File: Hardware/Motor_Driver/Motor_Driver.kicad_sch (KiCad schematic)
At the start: 16 parts, among them J1 Conn_SENSORS, J2 Conn_MOTOR, J3 Conn_MB, J4 Conn_PWR, Q1 CSD87333Q3D, Q2 CSD87333Q3D, Q3 CSD87333Q3D, U1 DRV8323SRTAR

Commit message: Day 4
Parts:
- removed Q1, Q2, Q3: CSD87333Q3D, Package_SON:VSON-8-1EP_3x3mm_P0.65mm_EP1.65x2.4mm, symbol Transistor_FET:DMN32D2LDF
- removed U1: DRV8323SRTAR, RTA0040B, symbol Driver_Motor:DRV8323SRTAR
- added C10, C11, C12, C13, C14, C15, C7, C8, C9: 4.7uF, symbol Device:C
- added C16, C17: C, symbol Device:C
- added D1: D_Schottky, symbol Device:D_Schottky
- added L1: L, symbol Device:L
- added Q1, Q2, Q3: CSD87333Q3D, Package_TO_SOT_SMD:SOT-353_SC-70-5, symbol Transistor_FET:CSD87333Q3D
- added R3, R4: R, symbol Device:R
- added U1: DRV8323RSRGZR, RTA0040B, symbol Driver_Motor:DRV8323RSRGZR
- C1, C2, C3, C5, C6, R1, R2: footprint (none) -> Capacitor_SMD:C_0402_1005Metric
- C4: footprint (none) -> Capacitor_SMD:C_0603_1608Metric
- J1: footprint (none) -> Connector_JST:JST_ZH_B6B-ZR_1x06_P1.50mm_Vertical
- J2: footprint (none) -> Connector_Pin:Pin_Bullet_D4.7mm
- J3: footprint (none) -> Connector_PinHeader_2.54mm:PinHeader_2x06_P2.54mm_Vertical
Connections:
- net +3V3: now also C5.1, U1.26 (VREF), U1.34 (CAL), U1.36 (DVDD); no longer J3.1 (Pin_1)
- net +5V: now also J3.1 (Pin_1), C17.1, L1.2, R3.1
- net BRAKE: now also U1.42 (INLC)
- net CLK: now also U1.31 (SCLK)
- net CS: now also U1.32 (nSCS)
- net DIR: now also U1.41 (INHC)
- net EN: now also U1.33 (ENABLE)
- net FAULT: now also U1.28 (nFAULT)
- net GND: now also C10.2, C11.2, C12.2, C13.2, C14.2, C15.2, C7.2, C8.2, C9.2, D1.2 (A), Q1.9 (P_{GND}), Q2.9 (P_{GND}), Q3.9 (P_{GND}), R4.2, U1.2 (PGND), U1.27 (DGND), U1.35 (AGND), U1.43 (BGND)
- net HALL_A: now also U1.38 (INLA)
- net HALL_B: now also U1.39 (INHB)
- net HALL_C: now also U1.40 (INLB)
- net PWM: now also U1.37 (INHA)
- net SDI: now also U1.30 (SDI)
- net SDO: now also U1.29 (SDO)
- net VM: now reaches C2.1, C3.1, C4.1, J4.1 (Pin_1)
- net VM: now also C10.1, C11.1, C12.1, C13.1, C14.1, C15.1, C7.1, C8.1, C9.1, Q1.1 (V_{IN}), Q1.2 (V_{IN}), Q2.1 (V_{IN}), Q2.2 (V_{IN}), Q3.1 (V_{IN}), Q3.2 (V_{IN}), U1.6 (VM), U1.7 (VDRAIN)
- net at J2.2 (Pin_2): now also Q2.6 (V_{SW}), Q2.7 (V_{SW}), Q2.8 (V_{SW})
- net at C1.1: now also U1.4 (CPH)
- net at C1.2: now also U1.3 (CPL)
- net at J2.1 (Pin_1): now also Q1.6 (V_{SW}), Q1.7 (V_{SW}), Q1.8 (V_{SW})
- net at J2.3 (Pin_3): now also Q3.6 (V_{SW}), Q3.7 (V_{SW}), Q3.8 (V_{SW})
- net at C2.2: now also U1.5 (VCP)
- new net: R3.2, R4.1, U1.1 (FB)
- new net: Q1.3 (T_{G}), U1.8 (GHA)
- new net: Q1.4 (T_{GR}), U1.9 (SHA)
- new net: Q1.5 (B_{G}), U1.10 (GLA)
- new net: Q2.5 (B_{G}), U1.15 (GLB)
- new net: Q2.4 (T_{GR}), U1.16 (SHB)
- new net: Q2.3 (T_{G}), U1.17 (GHB)
- new net: Q3.3 (T_{G}), U1.18 (GHC)
- new net: Q3.4 (T_{GR}), U1.19 (SHC)
- new net: Q3.5 (B_{G}), U1.20 (GLC)
- new net: C16.1, U1.44 (CB)
- new net: C16.2, D1.1 (K), L1.1, U1.45 (SW)
- no-connect marks 9 -> 10
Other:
- moved on the sheet: J1

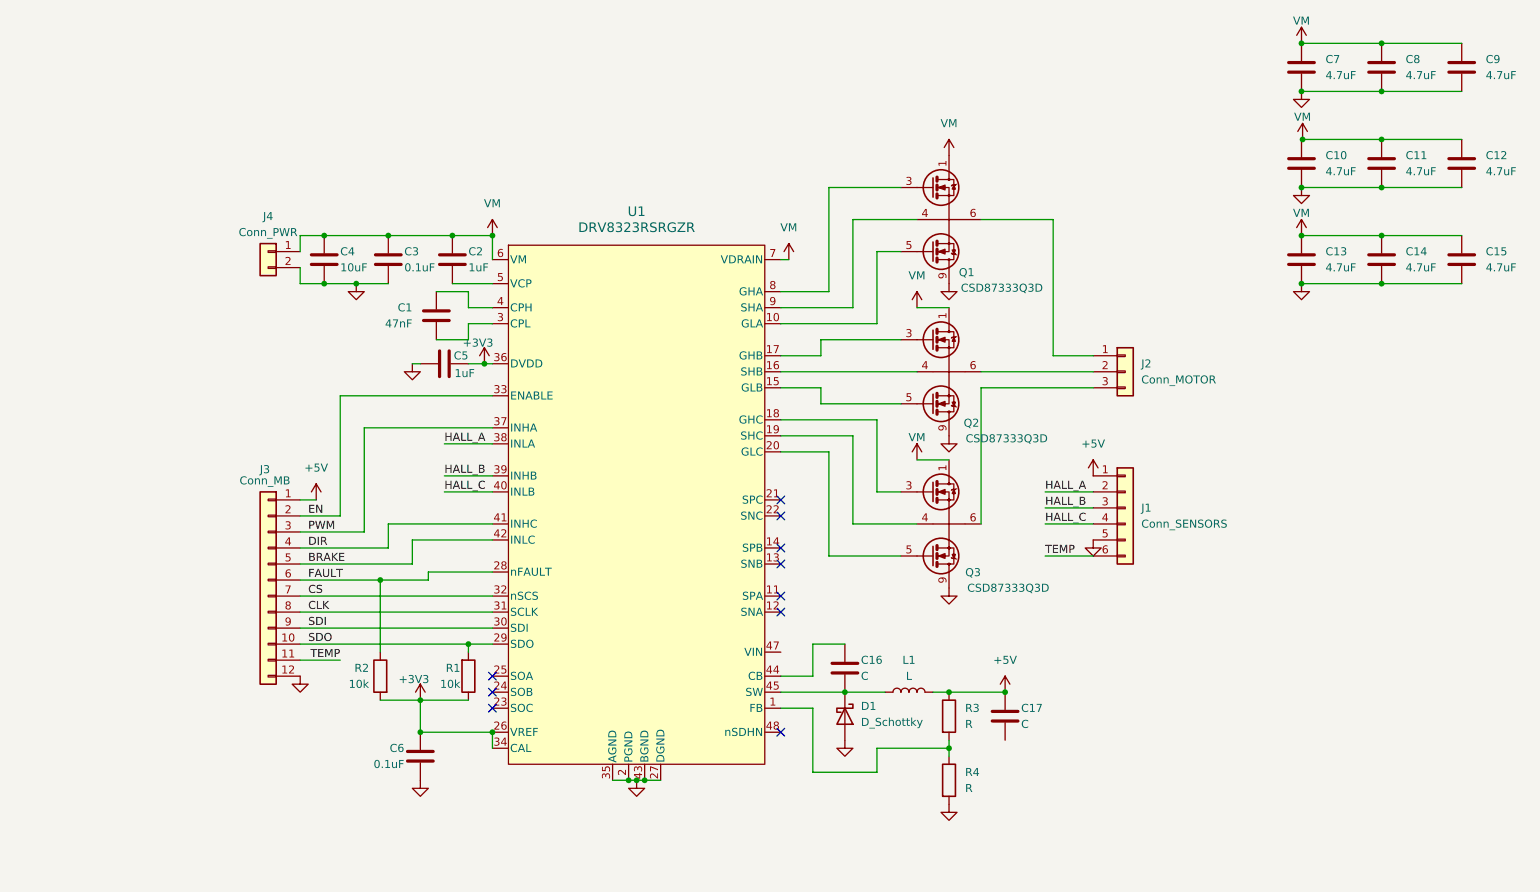
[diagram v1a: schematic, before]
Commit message: Day 5 - Finish motor driver PCB
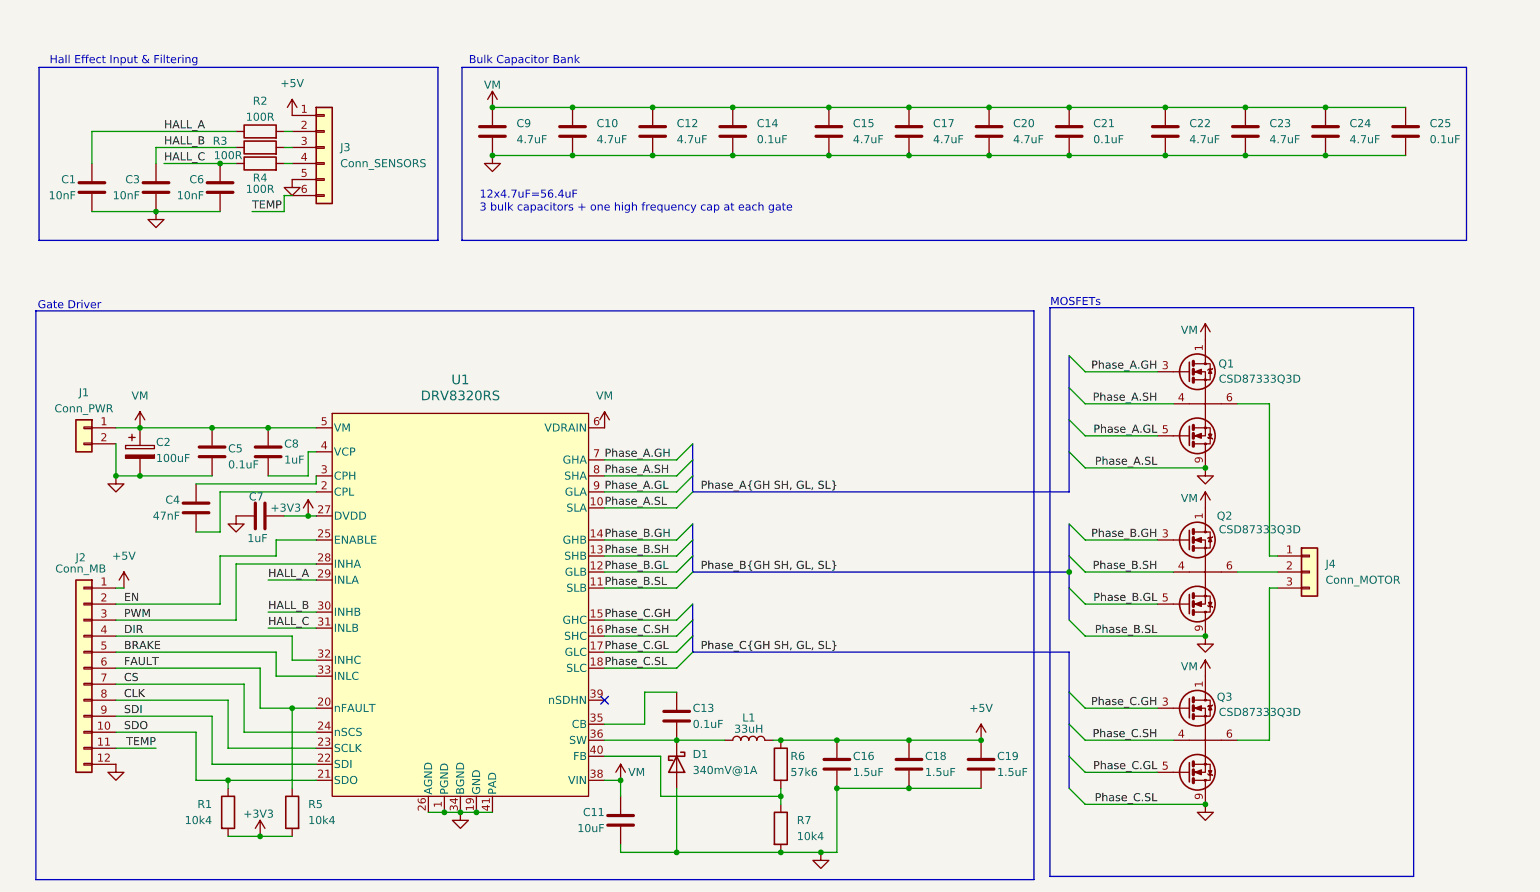
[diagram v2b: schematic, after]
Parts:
- removed C2: 1uF, Capacitor_SMD:C_0402_1005Metric, symbol Device:C
- removed U1: DRV8323RSRGZR, RTA0040B, symbol Driver_Motor:DRV8323RSRGZR
- added C11: 10uF, Capacitor_SMD:C_0603_1608Metric, symbol Device:C
- added C14, C21, C25: 0.1uF, Capacitor_SMD:C_0603_1608Metric, symbol Device:C
- added C18, C19: 1.5uF, Capacitor_SMD:C_0603_1608Metric, symbol Device:C
- added C2: 100uF, Capacitor_SMD:CP_Elec_10x10, symbol Device:C_Polarized
- added C7, C8: 1uF, Capacitor_SMD:C_0603_1608Metric, symbol Device:C
- added R3, R4: 100R, Resistor_SMD:R_0603_1608Metric, symbol Device:R
- added R5: 10k4, Resistor_SMD:R_0603_1608Metric, symbol Device:R
- added U1: DRV8320RS, Package_DFN_QFN:VQFN-40-1EP_6x6mm_P0.5mm_EP3.5x3.5mm_ThermalVias, symbol Driver_Motor:DRV8320RS
- C1: value 47nF -> 10nF; footprint Capacitor_SMD:C_0402_1005Metric -> Capacitor_SMD:C_0603_1608Metric; MPN (none) -> CL10B103KO8WPNC
- C10: renamed from C14; footprint (none) -> Capacitor_SMD:C_0603_1608Metric; MPN (none) -> CL10A475KO8NNNC
- C12: renamed from C15; footprint (none) -> Capacitor_SMD:C_0603_1608Metric; MPN (none) -> CL10A475KO8NNNC
- C13: renamed from C16; value C -> 0.1uF; footprint (none) -> Capacitor_SMD:C_0603_1608Metric; MPN (none) -> CC0603KRX7R7BB104
- C15: renamed from C7; footprint (none) -> Capacitor_SMD:C_0603_1608Metric; MPN (none) -> CL10A475KO8NNNC
- C16: renamed from C17; value C -> 1.5uF; footprint (none) -> Capacitor_SMD:C_0603_1608Metric; MPN (none) -> CL10A225KQ8NNWC
- C17: renamed from C8; footprint (none) -> Capacitor_SMD:C_0603_1608Metric; MPN (none) -> CL10A475KO8NNNC
- C20: renamed from C9; footprint (none) -> Capacitor_SMD:C_0603_1608Metric; MPN (none) -> CL10A475KO8NNNC
- C22: renamed from C10; footprint (none) -> Capacitor_SMD:C_0603_1608Metric; MPN (none) -> CL10A475KO8NNNC
- C23: renamed from C11; footprint (none) -> Capacitor_SMD:C_0603_1608Metric; MPN (none) -> CL10A475KO8NNNC
- C24: renamed from C12; footprint (none) -> Capacitor_SMD:C_0603_1608Metric; MPN (none) -> CL10A475KO8NNNC
- C3, C6: value 0.1uF -> 10nF; footprint Capacitor_SMD:C_0402_1005Metric -> Capacitor_SMD:C_0603_1608Metric; MPN (none) -> CL10B103KO8WPNC
- C4: value 10uF -> 47nF; MPN (none) -> https://www.digikey.ca/en/products/detail/samsung-electro-m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
- C5: value 1uF -> 0.1uF; footprint Capacitor_SMD:C_0402_1005Metric -> Capacitor_SMD:C_0603_1608Metric; MPN (none) -> CC0603KRX7R7BB104
- C9: renamed from C13; footprint (none) -> Capacitor_SMD:C_0603_1608Metric; MPN (none) -> CL10A475KO8NNNC
- D1: value D_Schottky -> 340mV@1A; footprint (none) -> Diode_SMD:Nexperia_CFP3_SOD-123W; MPN (none) -> PMEG2010ER,115
- J1: renamed from J4; footprint (none) -> Connector_Wire:SolderWirePad_1x02_SMD_5x10mm
- J2: renamed from J3; MPN (none) -> PPPC062LFBN-RC
- J3: renamed from J1; footprint Connector_JST:JST_ZH_B6B-ZR_1x06_P1.50mm_Vertical -> Connector_JST:JST_XH_B6B-XH-A_1x06_P2.50mm_Vertical; MPN (none) -> B6B-XH-A
- L1: value L -> 33uH; footprint (none) -> Inductor_SMD:L_10.4x10.4_H4.8; MPN (none) -> SRU1048-330Y
- Q1, Q2, Q3: footprint Package_TO_SOT_SMD:SOT-353_SC-70-5 -> Package_SON:VSON-8-1EP_3x3mm_P0.65mm_EP1.65x2.4mm_ThermalVias; MPN (none) -> CSD87333Q3D
- R1: value 10k -> 10k4; footprint Capacitor_SMD:C_0402_1005Metric -> Resistor_SMD:R_0603_1608Metric; MPN (none) -> RT0603BRD0710K4L
- R2: value 10k -> 100R; footprint Capacitor_SMD:C_0402_1005Metric -> Resistor_SMD:R_0603_1608Metric; MPN (none) -> RMCF0603JT100R
- R6: renamed from R3; value R -> 57k6; footprint (none) -> Resistor_SMD:R_0603_1608Metric; MPN (none) -> RC0603FR-0757K6L
- R7: renamed from R4; value R -> 10k4; footprint (none) -> Resistor_SMD:R_0603_1608Metric; MPN (none) -> RT0603BRD0710K4L
- renumbered J2 to J4
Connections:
- net +3V3: now also R1.2, C7.1, R5.2, U1.27 (DVDD); no longer C5.1, C6.1, R1.1, R2.2
- net +5V: now also C18.1, C19.1
- net BRAKE: now also U1.33 (INLC)
- net CLK: now also U1.23 (SCLK)
- net CS: now also U1.24 (nSCS)
- net DIR: now also U1.32 (INHC)
- net EN: now also U1.25 (ENABLE)
- net FAULT: now also R5.1, U1.20 (nFAULT); no longer R2.1
- net GND: now also C1.2, C16.2, C11.2, C14.2, C18.2, C19.2, C2.2, C21.2, C25.2, C7.2, U1.1 (PGND), U1.10 (SLA), U1.11 (SLB), U1.18 (SLC), U1.19 (GND), U1.26 (AGND), U1.34 (BGND), U1.41 (PAD); no longer C4.2
- net HALL_A: now also C1.1, R2.1, U1.29 (INLA); no longer J3.2 (Pin_2)
- net HALL_B: now also C3.1, R3.1, U1.30 (INHB); no longer J3.3 (Pin_3)
- net HALL_C: now also C6.1, R4.1, U1.31 (INLB); no longer J3.4 (Pin_4)
- net PWM: now also U1.28 (INHA)
- net SDI: now also U1.22 (SDI)
- net SDO: now also R1.1, U1.21 (SDO); no longer R1.2
- net VM: now also C5.1, C11.1, C14.1, C2.1, C21.1, C25.1, C8.1, U1.38 (VIN), U1.5 (VM), U1.6 (VDRAIN); no longer C3.1, C4.1
- net at R6.2, R7.1: now also U1.40 (FB)
- net Phase_A.GH: now reaches Q1.3 (T_{G})
- net Phase_A.GH: now also U1.7 (GHA)
- net Phase_A.SH: now reaches Q1.4 (T_{GR})
- net Phase_A.SH: now also U1.8 (SHA)
- net Phase_A.GL: now reaches Q1.5 (B_{G})
- net Phase_A.GL: now also U1.9 (GLA)
- net Phase_B.GL: now reaches Q2.5 (B_{G})
- net Phase_B.GL: now also U1.12 (GLB)
- net Phase_B.SH: now reaches Q2.4 (T_{GR})
- net Phase_B.SH: now also U1.13 (SHB)
- net Phase_B.GH: now reaches Q2.3 (T_{G})
- net Phase_B.GH: now also U1.14 (GHB)
- net Phase_C.GH: now reaches Q3.3 (T_{G})
- net Phase_C.GH: now also U1.15 (GHC)
- net Phase_C.SH: now reaches Q3.4 (T_{GR})
- net Phase_C.SH: now also U1.16 (SHC)
- net Phase_C.GL: now reaches Q3.5 (B_{G})
- net Phase_C.GL: now also U1.17 (GLC)
- net at C13.1: now also U1.35 (CB)
- net at C13.2, D1.1 (K), L1.1: now also U1.36 (SW)
- new net: C4.1, U1.3 (CPH)
- new net: C4.2, U1.2 (CPL)
- new net: C8.2, U1.4 (VCP)
- new net: J3.2 (Pin_2), R2.2
- new net: J3.3 (Pin_3), R3.2
- new net: J3.4 (Pin_4), R4.2
- no-connect marks 10 -> 1
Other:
- note added: "12x4.7uF=56.4uF 3 bulk capacitors + one high frequency cap at each gate"
- note added: "Bulk Capacitor Bank"
- note added: "Gate Driver"
- note added: "Hall Effect Input & Filtering"
- note added: "MOSFETs"
- company: (none) -> Designed by Adam Turaj
- title: (none) -> Sensored Brushless Motor ESC
- moved on the sheet: C10, C12, C13, C15, C16, C17, C20, C22, C23, C24, C9, D1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

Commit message: Day 6
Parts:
- removed C14, C21, C25: 0.1uF, Capacitor_SMD:C_0603_1608Metric, symbol Device:C
- removed C2: 100uF, Capacitor_SMD:CP_Elec_10x10, symbol Device:C_Polarized
- removed J2: Conn_MB, Connector_PinHeader_2.54mm:PinHeader_2x06_P2.54mm_Vertical, symbol Connector_Generic:Conn_01x12
- removed Q1, Q2, Q3: CSD87333Q3D, Package_SON:VSON-8-1EP_3x3mm_P0.65mm_EP1.65x2.4mm_ThermalVias, symbol Transistor_FET:CSD87333Q3D
- added C14, C21, C25: 150uF, symbol Device:C_Polarized
- added C2: 10uF, Capacitor_SMD:C_0603_1608Metric, symbol Device:C
- added J2: Conn_MB, Connector_PinSocket_2.54mm:PinSocket_2x08_P2.54mm_Vertical, symbol Connector_Generic:Conn_01x16
- added Q1, Q2, Q3: HP8K22TB, Package_SO:HSOP-8-1EP_3.9x4.9mm_P1.27mm_EP2.41x3.1mm_ThermalVias, symbol Transistor_FET:HP8K22TB
- added TP1, TP10, TP11, TP2, TP3, TP4, TP5, TP6, TP7, TP8, TP9: TestPoint, TestPoint:TestPoint_Pad_D1.0mm, symbol Connector:TestPoint
- J1: footprint Connector_Wire:SolderWirePad_1x02_SMD_5x10mm -> Connector_AMASS:AMASS_XT60PW-M_1x02_P7.20mm_Horizontal
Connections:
- net +3V3: now also TP8.1
- net +5V: now also J2.2 (Pin_2), TP7.1
- net BRAKE: now also J2.6 (Pin_6)
- net CLK: now also J2.9 (Pin_9)
- net CS: now also J2.8 (Pin_8)
- net DIR: now also J2.5 (Pin_5)
- net EN: now also J2.3 (Pin_3)
- net FAULT: now also J2.7 (Pin_7)
- net GND: now also C14.2, C2.2, C21.2, C25.2, J2.16 (Pin_16), Q1.5 (P_{GND}), Q1.6 (P_{GND}), Q1.7 (P_{GND}), Q2.5 (P_{GND}), Q2.6 (P_{GND}), Q2.7 (P_{GND}), Q3.5 (P_{GND}), Q3.6 (P_{GND}), Q3.7 (P_{GND})
- net HALL_A: now also J2.13 (Pin_13), TP9.1
- net HALL_B: now also J2.14 (Pin_14), TP10.1
- net HALL_C: now also J2.15 (Pin_15), TP11.1
- net PWM: now also J2.4 (Pin_4)
- net Phase_A.GH: now also Q1.1 (T_{G}), TP1.1
- net Phase_A.GL: now also Q1.8 (B_{G}), TP2.1
- net Phase_A.SH: now also Q1.9 (V_{SW})
- net Phase_B.GH: now also Q2.1 (T_{G}), TP3.1
- net Phase_B.GL: now also Q2.8 (B_{G}), TP4.1
- net Phase_B.SH: now also Q2.9 (V_{SW})
- net Phase_C.GH: now also Q3.1 (T_{G}), TP5.1
- net Phase_C.GL: now also Q3.8 (B_{G}), TP6.1
- net Phase_C.SH: now also Q3.9 (V_{SW})
- net SDI: now also J2.10 (Pin_10)
- net SDO: now also J2.11 (Pin_11)
- net TEMP: now also J2.12 (Pin_12)
- net VM: now also C14.1, C2.1, C21.1, C25.1, J2.1 (Pin_1), Q1.2 (V_{IN}), Q1.3 (V_{IN}), Q1.4 (V_{IN}), Q2.2 (V_{IN}), Q2.3 (V_{IN}), Q2.4 (V_{IN}), Q3.2 (V_{IN}), Q3.3 (V_{IN}), Q3.4 (V_{IN})
- net at J4.2 (Pin_2): now also Q2.9 (V_{SW})
- net at J4.1 (Pin_1): now also Q1.9 (V_{SW})
- net at J4.3 (Pin_3): now also Q3.9 (V_{SW})
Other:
- note added: "Minimum Bulk Capacitance (Rule of thumb is 20uF per 1A): 20uF*25A=~500uF One 150uF + three 4.7uF per phase 150uF*3 + 4.7uF*9=492.3uF (As the above equation is just a rule of thumb, this will work well)"
- note removed: "12x4.7uF=56.4uF 3 bulk capacitors + one high frequency cap at each gate"
- moved on the sheet: C10, C12, C15, C17, C20, C22, C23, C24, C9
